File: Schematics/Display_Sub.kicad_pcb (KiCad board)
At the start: 2 copper layers, 17 x 24 mm, 20 parts, among them P1 CONN_01X04, P2 CONN_01X04, P3 CONN_01X04, P4 CONN_01X04, P5 CONN_01X04, P6 CONN_01X06, U1 PCA9685

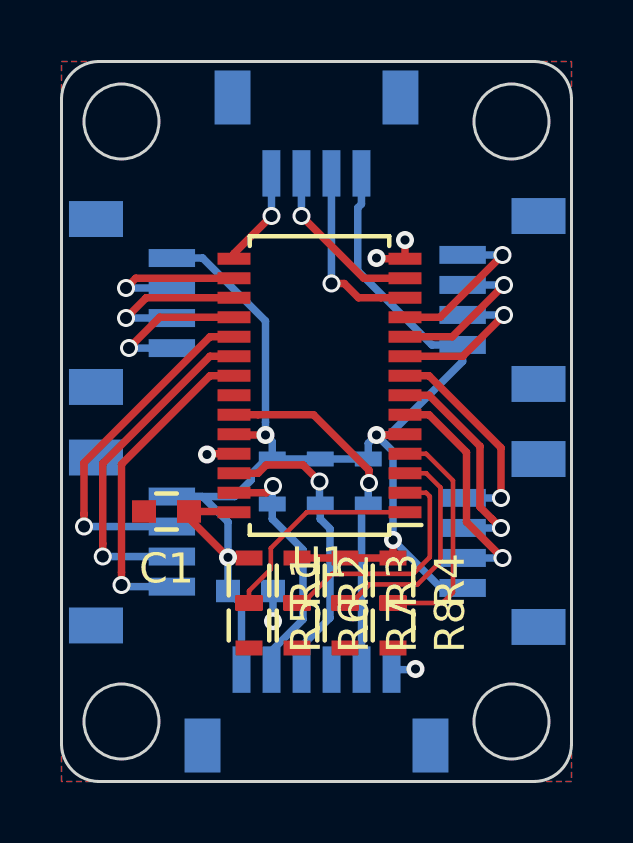
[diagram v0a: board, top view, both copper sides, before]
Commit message: Sorted silkscreen out and panelized design.
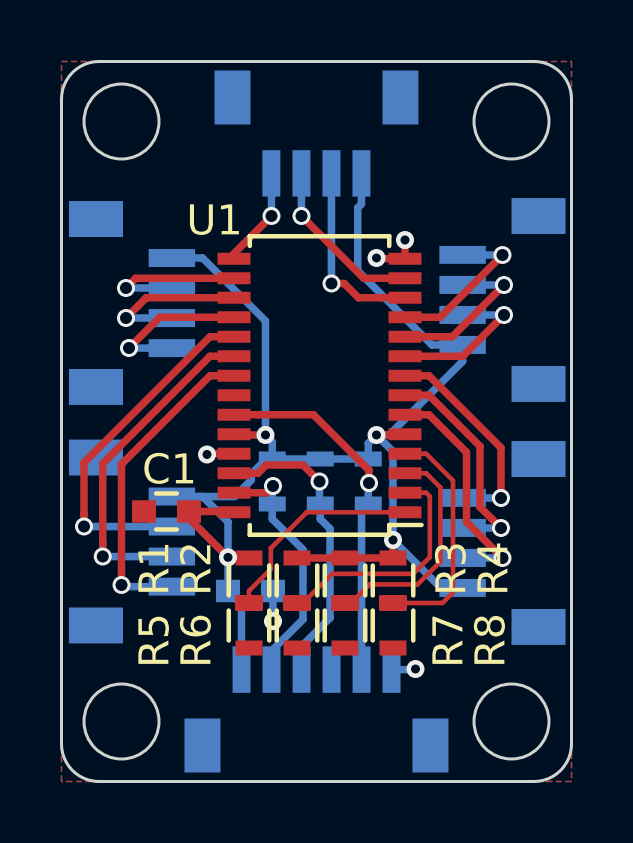
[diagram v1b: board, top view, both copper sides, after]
